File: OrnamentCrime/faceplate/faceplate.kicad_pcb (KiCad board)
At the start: 2 copper layers, 70.8 x 128.4 mm, 17 parts

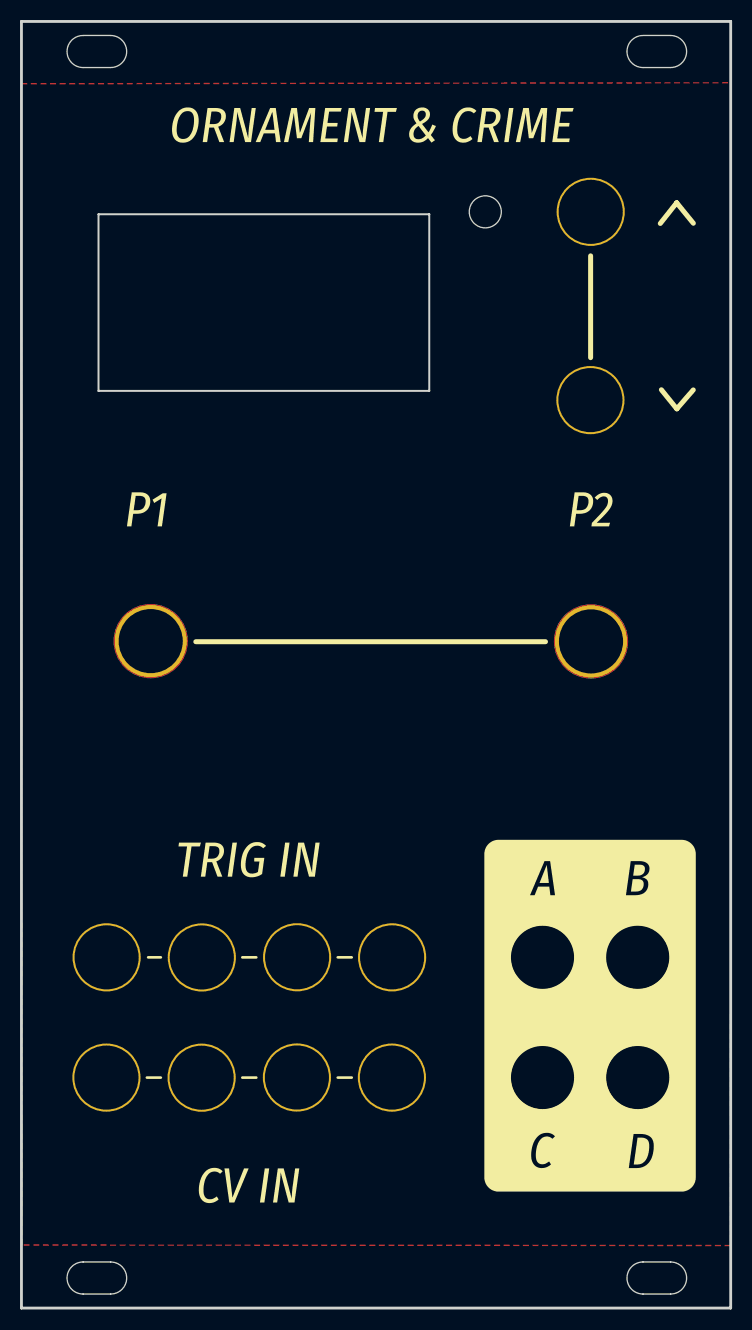
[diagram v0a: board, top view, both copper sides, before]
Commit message: Add USB header to O&C face plate
Because some of the alternative firmwares provide USB HOST.

We'll figure out if a diode is enough to power it.
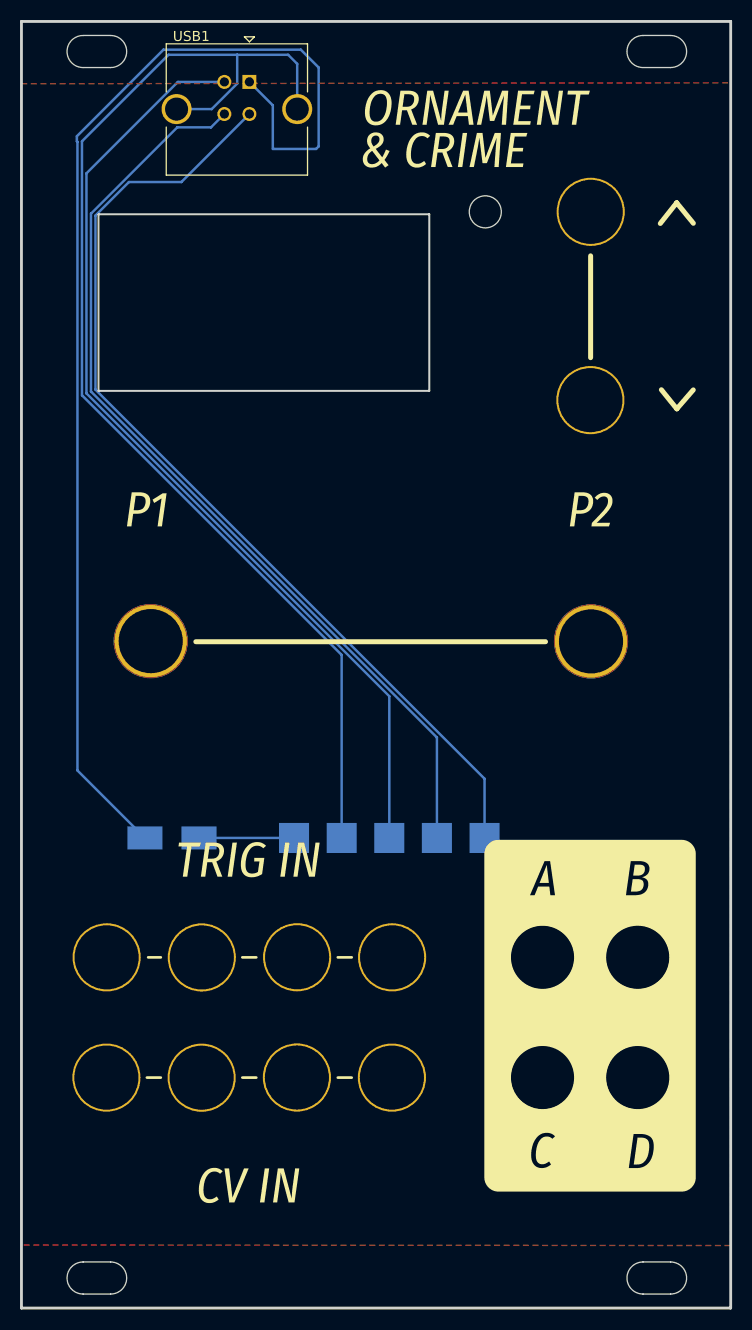
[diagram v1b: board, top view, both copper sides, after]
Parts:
- added D1: D_Schottky, Diode_SMD:D_SMB_Handsoldering, B.Cu at (78.1, 108.4)
- added J1: Conn_01x01_Female, TestPoint:TestPoint_Pad_3.0x3.0mm, B.Cu at (95.0, 108.4)
- added J3: Conn_01x01_Female, TestPoint:TestPoint_Pad_3.0x3.0mm, B.Cu at (109.3, 108.4)
- added J4: Conn_01x01_Female, TestPoint:TestPoint_Pad_3.0x3.0mm, B.Cu at (104.5, 108.4)
- added J5: Conn_01x01_Female, TestPoint:TestPoint_Pad_3.0x3.0mm, B.Cu at (99.8, 108.4)
- added J6: Conn_01x01_Female, TestPoint:TestPoint_Pad_3.0x3.0mm, B.Cu at (90.3, 108.4)
- added USB1: USB_B, Connector_USB:USB_B_TE_5787834_Vertical, F.Cu at (85.8, 32.9)
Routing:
- net Net-(D1-Pad2): track 0.00 -> 121.5 mm
- net /SHIELD: track 0.00 -> 120.2 mm
- net /GND: track 0.00 -> 97.8 mm
- net /D-: track 0.00 -> 96.4 mm
- net /D+: track 0.00 -> 94.0 mm
- net /VBUS: track 0.00 -> 9.48 mm
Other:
- board text added: "D+"
- board text added: "D-"
- board text added: "GND"
- board text added: "USB"
- board text added: "Vbus"
- board text added: "shield"
